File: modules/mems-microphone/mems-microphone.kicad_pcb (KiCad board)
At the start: 2 copper layers, 13.2 x 14.3 mm, 6 parts

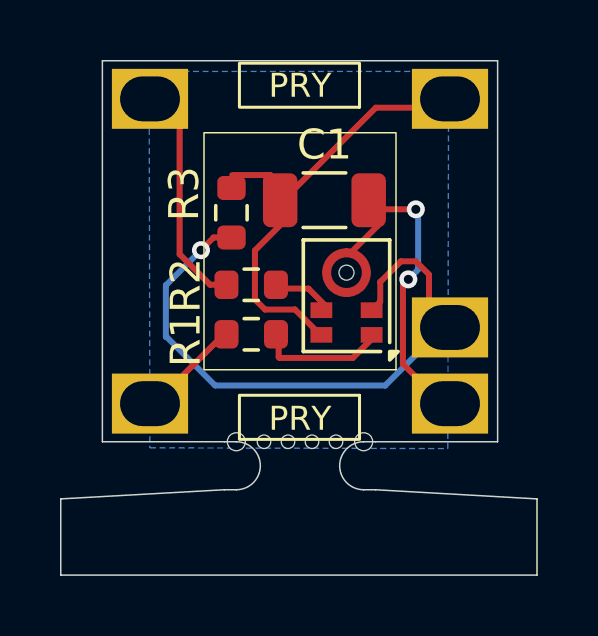
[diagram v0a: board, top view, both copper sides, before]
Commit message: Updating mems mic
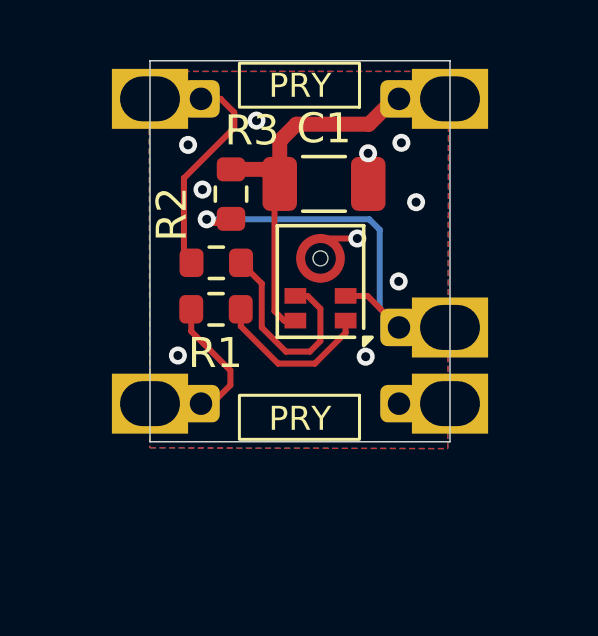
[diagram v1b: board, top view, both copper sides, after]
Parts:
- M1: footprint MegaCastle:MegaCastle2x5-Module-I6.4x7.9-M9C4-PANEL-NIBBLE -> MegaCastle:MegaCastle2x5-Module-I10.0x7.9-M9C4-SPAREPAD
- moved R1 1.44 mm to (59.1, 49.6)
- moved R2 1.37 mm to (59.2, 48.0)
- moved MK1 0.99 mm to (62.6, 48.6)
- moved R3 0.62 mm to (59.6, 45.7)
- moved C1 0.54 mm to (62.8, 45.4)
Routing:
- net GND: track 11.6 -> 2.25 mm, vias 2 -> 9
- net LR_SELECT: track 22.4 -> 14.7 mm
- net Net-(MK1-CLOCK): track 2.01 -> 6.97 mm
- net VCC: track 15.6 -> 13.0 mm
- net Net-(MK1-DATA): track 4.42 -> 5.41 mm
- net DATA: track 3.67 -> 4.31 mm
- net CLOCK: track 7.68 -> 7.11 mm
- net (no net): vias 0 -> 1
- added copper zone on F.Cu, net GND
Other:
- board size 13.2 x 14.3 mm -> 10 x 12.7 mm
